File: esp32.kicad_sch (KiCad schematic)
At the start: 15 parts, among them J2 Conn_01x05_Pin, J3 PJ398SM-12, Q3 MMBT3904, Q4 MMBT3904, Y1 ECS-2520MV-xxx-xx

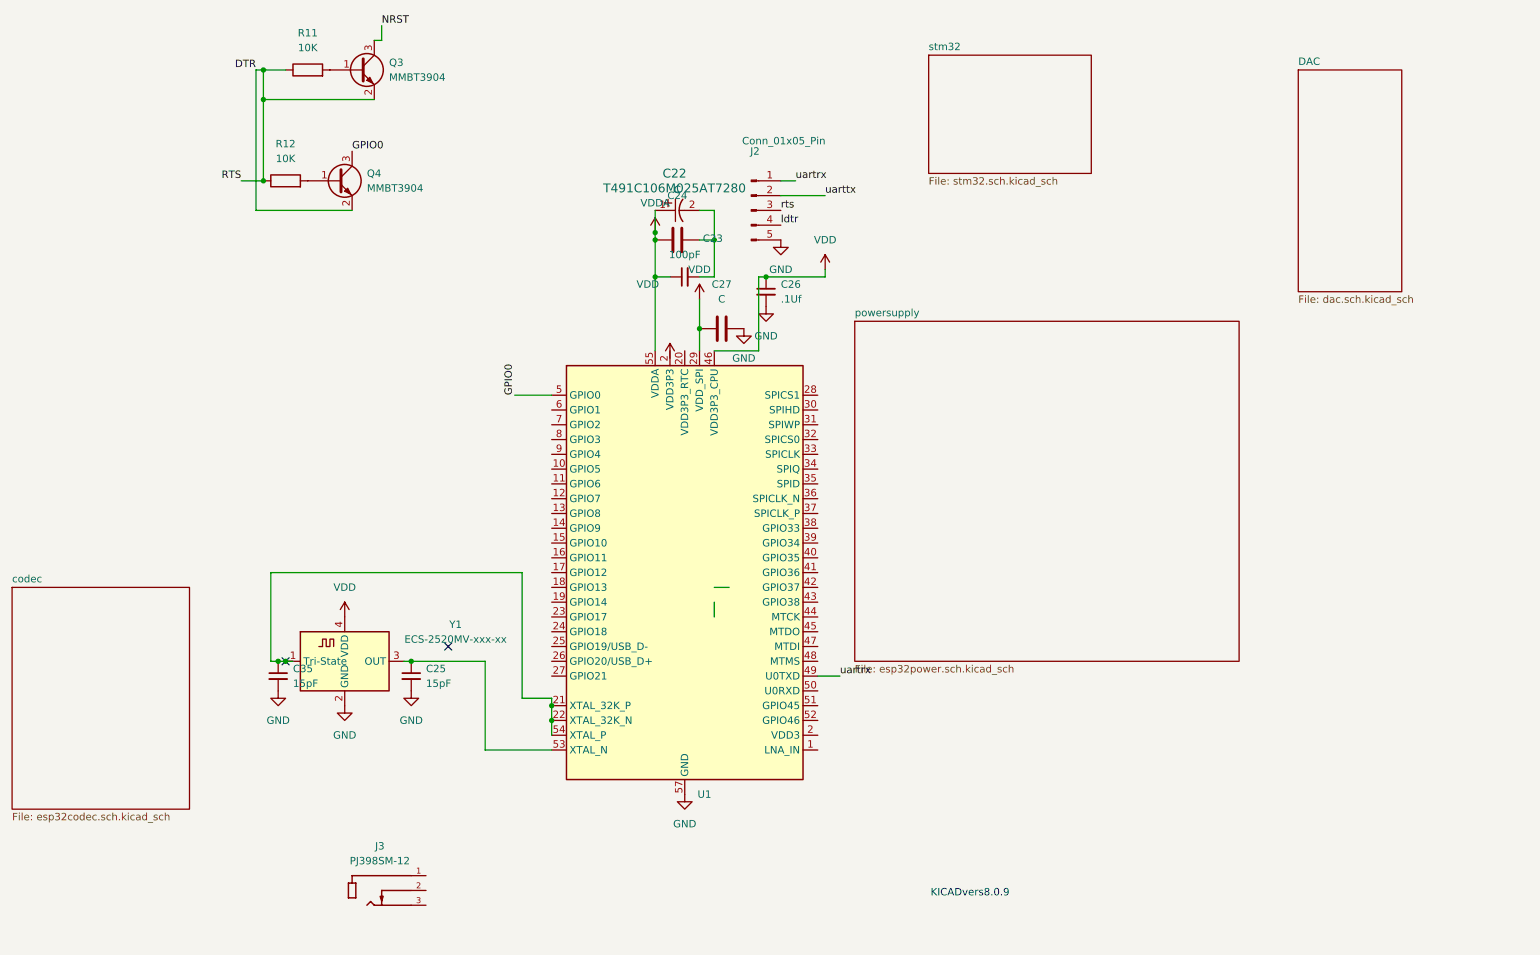
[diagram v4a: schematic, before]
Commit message: modelpathssdefuined
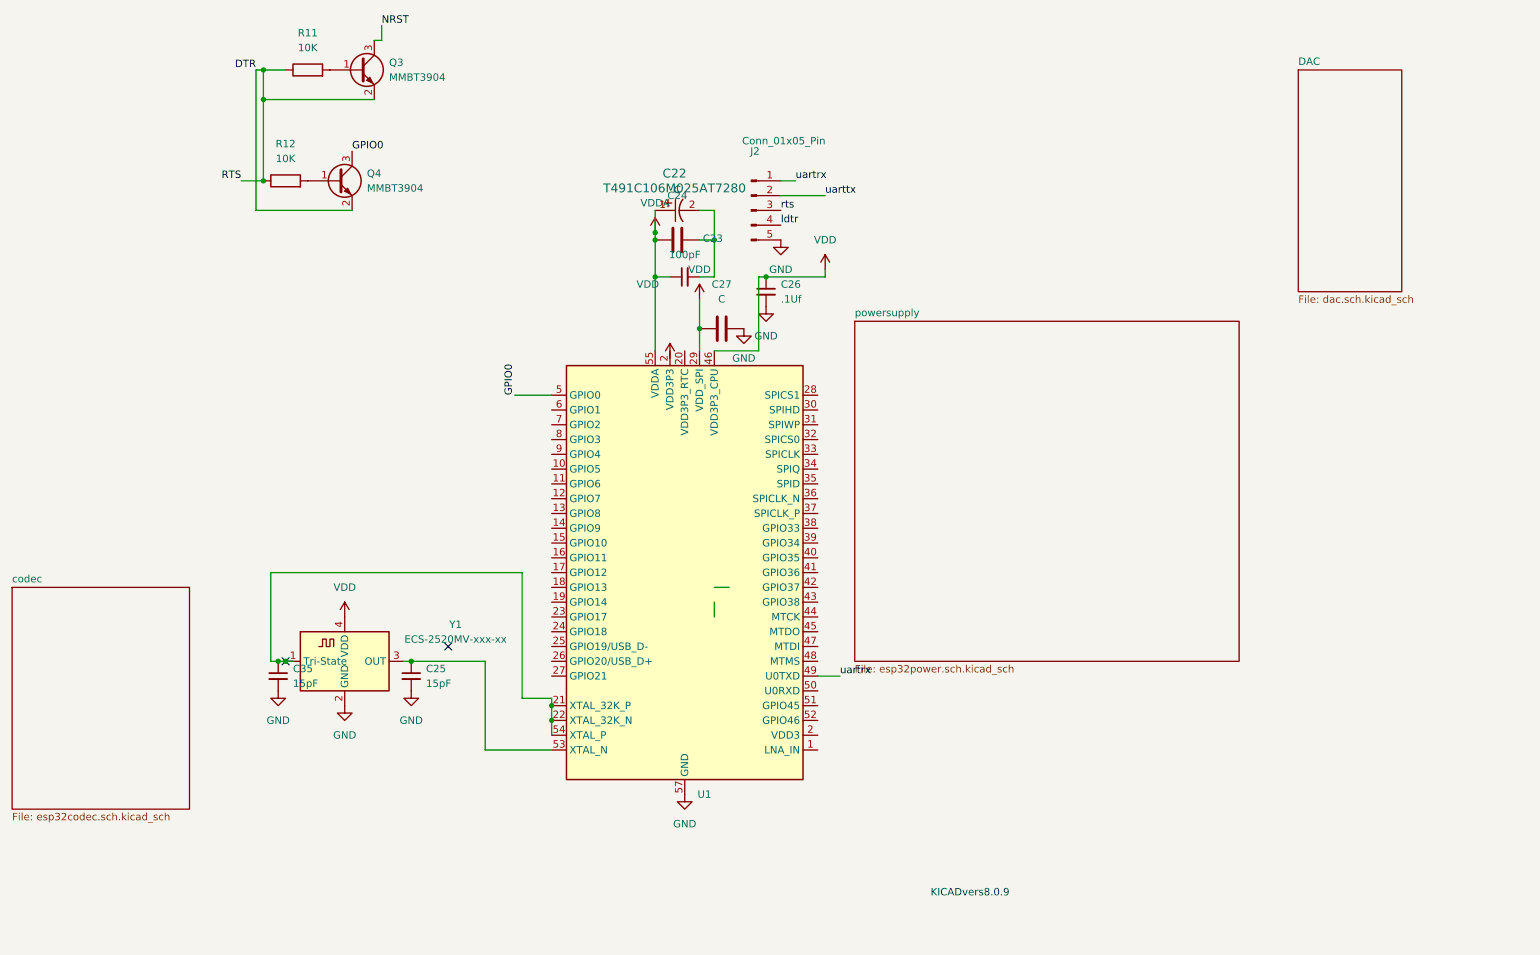
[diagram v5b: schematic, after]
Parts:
- removed J3: PJ398SM-12, customfootprints:THONK_PJ398SM-12, symbol esp32lib:PJ398SM-12
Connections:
- net at U1.2 (VDD3P3): now also U1.3 (VDD3P3)
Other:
- removed sheet stm32
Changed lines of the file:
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@@
-	)
-	(symbol
-		(lib_id "esp32lib:PJ398SM-12")
-		(at 86.36 168.91 0)
-		(unit 1)
-		(exclude_from_sim no)
-		(in_bom yes)
-		(on_board yes)
-		(dnp no)
-		(fields_autoplaced yes)
-		(property "Reference" "J3"
-			(at 86.0425 163.83 0)
-			(effects
-				(font
-					(size 1.27 1.27)
-				)
-			)
-		)
-		(property "Value" "PJ398SM-12"
-			(at 86.0425 166.37 0)
-			(effects
-				(font
-					(size 1.27 1.27)
-				)
-			)
-		)
-		(property "Footprint" "customfootprints:THONK_PJ398SM-12"
-			(at 86.36 168.91 0)
-			(effects
-				(font
-					(size 1.27 1.27)
-				)
-				(justify bottom)
-				(hide yes)
-			)
-		)
-		(property "Datasheet" ""
-			(at 86.36 168.91 0)
-			(effects
-				(font
-					(size 1.27 1.27)
-				)
-				(hide yes)
-			)
-		)
-		(property "Description" ""
-			(at 86.36 168.91 0)
-			(effects
-				(font
-					(size 1.27 1.27)
-				)
-				(hide yes)
-			)
-		)
-		(property "MF" "Thonk"
-			(at 86.36 168.91 0)
-			(effects
-				(font
-					(size 1.27 1.27)
-				)
-				(justify bottom)
-				(hide yes)
-			)
-		)
-		(property "MAXIMUM_PACKAGE_HEIGHT" "14.5 mm"
-			(at 86.36 168.91 0)
-			(effects
-				(font
-					(size 1.27 1.27)
-				)
-				(justify bottom)
-				(hide yes)
-			)
-		)
-		(property "Package" "Package"
-			(at 86.36 168.91 0)
-			(effects
-				(font
-					(size 1.27 1.27)
-				)
-				(justify bottom)
-				(hide yes)
-			)
-		)
-		(property "Price" "None"
-			(at 86.36 168.91 0)
-			(effects
-				(font
-					(size 1.27 1.27)
-				)
-				(justify bottom)
-				(hide yes)
-			)
-		)
-		(property "Check_prices" "https://www.snapeda.com/parts/PJ398SM-12/Thonk/view-part/?ref=eda"
-			(at 86.36 168.91 0)
-			(effects
-				(font
-					(size 1.27 1.27)
-				)
-				(justify bottom)
-				(hide yes)
-			)
-		)
-		(property "STANDARD" "Manufacturer Recommendations"
-			(at 86.36 168.91 0)
-			(effects
-				(font
-					(size 1.27 1.27)
-				)
-				(justify bottom)
-				(hide yes)
-			)
-		)
-		(property "PARTREV" "1"
-			(at 86.36 168.91 0)
-			(effects
-				(font
-					(size 1.27 1.27)
-				)
-				(justify bottom)
-				(hide yes)
-			)
-		)
-		(property "SnapEDA_Link" "https://www.snapeda.com/parts/PJ398SM-12/Thonk/view-part/?ref=snap"
-			(at 86.36 168.91 0)
-			(effects
-				(font
-					(size 1.27 1.27)
-				)
-				(justify bottom)
-				(hide yes)
-			)
-		)
-		(property "MP" "PJ398SM-12"
-			(at 86.36 168.91 0)
-			(effects
-				(font
-					(size 1.27 1.27)
-				)
-				(justify bottom)
-				(hide yes)
-			)
-		)
-		(property "Description_1" "\n                        \n                            3.5mm Switching Jack Socket\n                        \n"
-			(at 86.36 168.91 0)
-			(effects
-				(font
-					(size 1.27 1.27)
-				)
-				(justify bottom)
-				(hide yes)
-			)
-		)
-		(property "Availability" "Not in stock"
-			(at 86.36 168.91 0)
-			(effects
-				(font
-					(size 1.27 1.27)
-				)
-				(justify bottom)
-				(hide yes)
-			)
-		)
-		(property "MANUFACTURER" "Thonk"
-			(at 86.36 168.91 0)
-			(effects
-				(font
-					(size 1.27 1.27)
-				)
-				(justify bottom)
-				(hide yes)
-			)
-		)
-		(pin "3"
-		)
-		(pin "2"
-		)
-		(pin "1"
-		)
-		(instances
-			(project ""
-				(path "/c4754426-a41b-4341-9d09-2e389619f3d6"
-					(reference "J3")
-					(unit 1)
-				)
-			)
-		)
 	)
 	(symbol
@@
 				)
 			)
-		)
-	)
-	(sheet
-		(at 180.34 27.94)
-		(size 27.94 20.32)
-		(fields_autoplaced yes)
-		(stroke
-			(width 0.1524)
-			(type solid)
-		)
-		(fill
-			(color 0 0 0 0.0000)
-		)
-		(property "Sheetname" "stm32"
-			(at 180.34 27.2284 0)
-			(effects
-				(font
-					(size 1.27 1.27)
-				)
-				(justify left bottom)
-			)
-		)
-		(property "Sheetfile" "stm32.sch.kicad_sch"
-			(at 180.34 48.8446 0)
-			(effects
-				(font
-					(size 1.27 1.27)
-				)
-				(justify left top)
-			)
-		)
-		(instances
-			(project "esp32"
-				(path "/c4754426-a41b-4341-9d09-2e389619f3d6"
-					(page "6")
-				)
-			)

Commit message: improvedCVSumming buffers
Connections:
- net at U1.2 (VDD3P3): now also U1.3 (VDD3P3)
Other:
- added sheet ADCCVbuffer (CVBuffer.kicad_sch)
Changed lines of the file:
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@@
+	)
+	(sheet
+		(at 66.04 160.02)
+		(size 20.32 17.78)
+		(fields_autoplaced yes)
+		(stroke
+			(width 0.1524)
+			(type solid)
+		)
+		(fill
+			(color 0 0 0 0.0000)
+		)
+		(property "Sheetname" "ADCCVbuffer"
+			(at 66.04 159.3084 0)
+			(effects
+				(font
+					(size 1.27 1.27)
+				)
+				(justify left bottom)
+			)
+		)
+		(property "Sheetfile" "CVBuffer.kicad_sch"
+			(at 66.04 178.3846 0)
+			(effects
+				(font
+					(size 1.27 1.27)
+				)
+				(justify left top)
+			)
+		)
+		(instances
+			(project "esp32"
+				(path "/c4754426-a41b-4341-9d09-2e389619f3d6"
+					(page "10")
+				)
+			)
+		)
 	)
 	(sheet

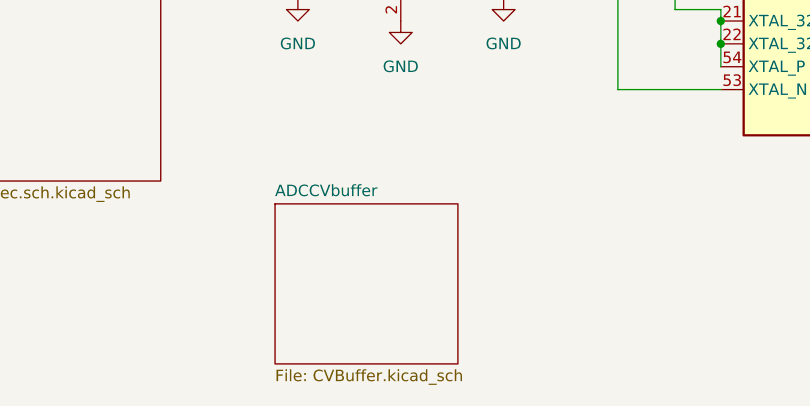
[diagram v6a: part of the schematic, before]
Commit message: added codec buffers
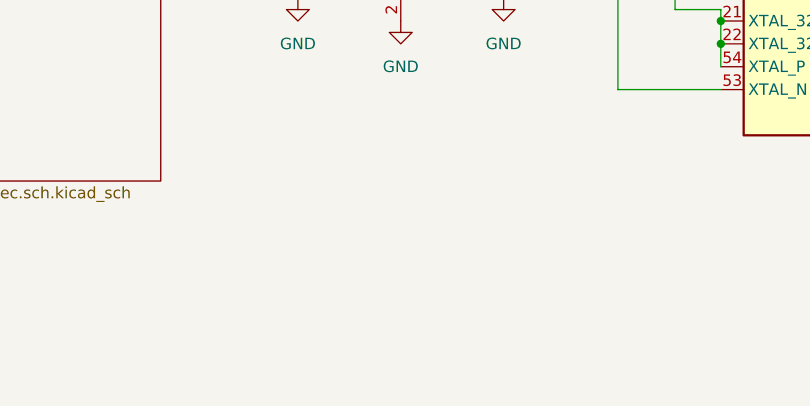
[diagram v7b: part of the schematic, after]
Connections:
- net at U1.2 (VDD3P3): now also U1.3 (VDD3P3)
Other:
- removed sheet ADCCVbuffer
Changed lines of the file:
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@@
-	)
-	(sheet
-		(at 66.04 160.02)
-		(size 20.32 17.78)
-		(fields_autoplaced yes)
-		(stroke
-			(width 0.1524)
-			(type solid)
-		)
-		(fill
-			(color 0 0 0 0.0000)
-		)
-		(property "Sheetname" "ADCCVbuffer"
-			(at 66.04 159.3084 0)
-			(effects
-				(font
-					(size 1.27 1.27)
-				)
-				(justify left bottom)
-			)
-		)
-		(property "Sheetfile" "CVBuffer.kicad_sch"
-			(at 66.04 178.3846 0)
-			(effects
-				(font
-					(size 1.27 1.27)
-				)
-				(justify left top)
-			)
-		)
-		(instances
-			(project "esp32"
-				(path "/c4754426-a41b-4341-9d09-2e389619f3d6"
-					(page "10")
-				)
-			)
-		)
 	)
 	(sheet

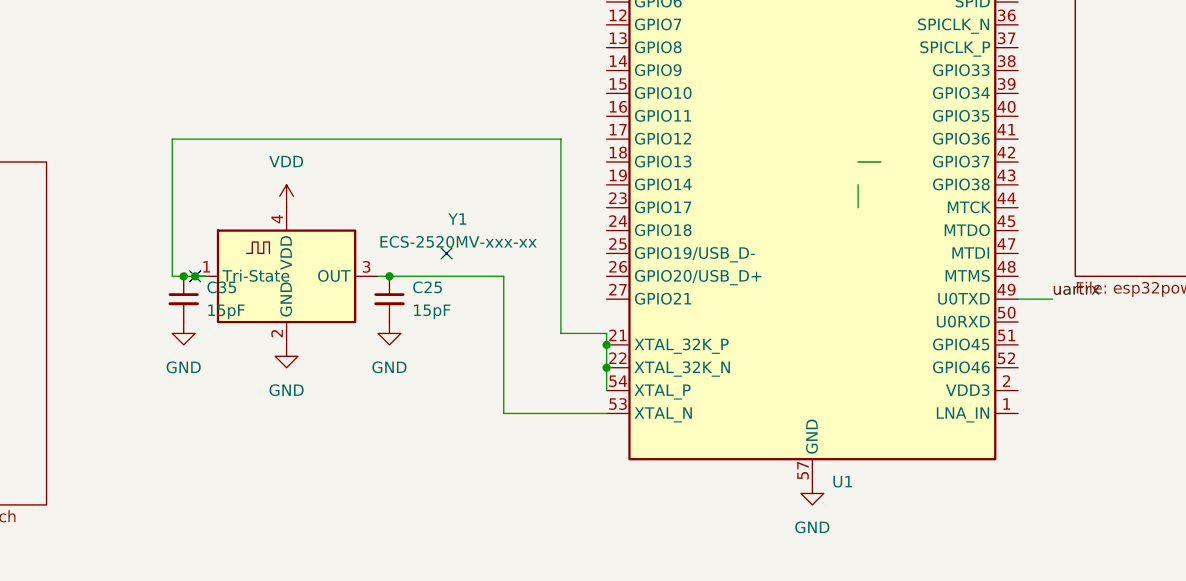
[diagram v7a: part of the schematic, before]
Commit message: added global library
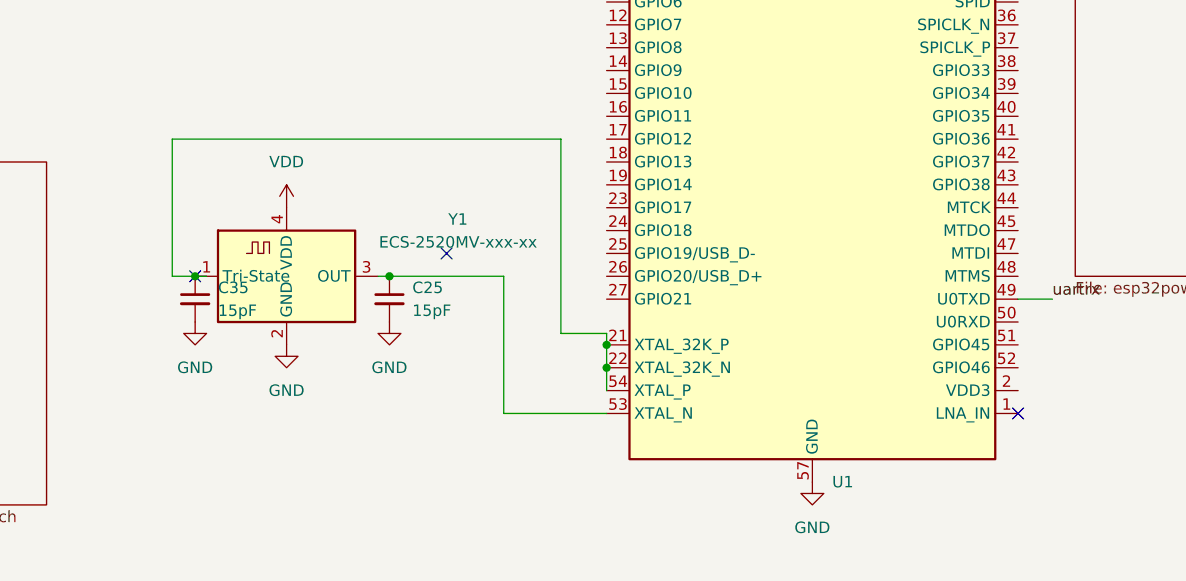
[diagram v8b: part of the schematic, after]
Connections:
- net at U1.2 (VDD3P3): now also U1.3 (VDD3P3)
- no-connect marks 2 -> 3
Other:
- moved on the sheet: C35
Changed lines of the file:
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@@
-	)
-	(junction
-		(at 68.58 132.08)
-		(diameter 0)
-		(color 0 0 0 0)
 	)
 	(junction
@@
 	)
 	(no_connect
+		(at 161.29 147.32)
+	)
+	(no_connect
 		(at 69.85 132.08)
 	)
@@
 	(wire
 		(pts
-			(xy 143.51 124.46) (xy 143.51 121.92)
-		)
-		(stroke
-			(width 0)
-			(type default)
-		)
-	)
-	(wire
-		(pts
 			(xy 133.35 59.69) (xy 133.35 66.04)
 		)
@@
 	(wire
 		(pts
-			(xy 146.05 119.38) (xy 143.51 119.38)
-		)
-		(stroke
-			(width 0)
-			(type default)
-		)
-	)
-	(wire
-		(pts
-			(xy 67.31 132.08) (xy 68.58 132.08)
+			(xy 67.31 132.08) (xy 69.85 132.08)
 		)
 		(stroke
@@
 		(pts
 			(xy 66.04 35.56) (xy 85.09 35.56)
-		)
-		(stroke
-			(width 0)
-			(type default)
-		)
-	)
-	(wire
-		(pts
-			(xy 68.58 132.08) (xy 69.85 132.08)
 		)
 		(stroke
@@
 	(symbol
 		(lib_id "Device:C_Small")
-		(at 68.58 134.62 0)
+		(at 69.85 134.62 0)
 		(unit 1)
 		(exclude_from_sim no)
@@
 		(fields_autoplaced yes)
 		(property "Reference" "C35"
-			(at 71.12 133.3562 0)
+			(at 72.39 133.3562 0)
 			(effects
 				(font
@@
 		)
 		(property "Value" "15pF"
-			(at 71.12 135.8962 0)
+			(at 72.39 135.8962 0)
 			(effects
 				(font
@@
 		)
 		(property "Footprint" "Capacitor_SMD:C_0201_0603Metric"
-			(at 68.58 134.62 0)
+			(at 69.85 134.62 0)
 			(effects
 				(font
@@
 		)
 		(property "Datasheet" "~"
-			(at 68.58 134.62 0)
+			(at 69.85 134.62 0)
 			(effects
 				(font
@@
 		)
 		(property "Description" "Unpolarized capacitor, small symbol"
-			(at 68.58 134.62 0)
+			(at 69.85 134.62 0)
 			(effects
 				(font
@@
 	(symbol
 		(lib_id "power:GND")
-		(at 68.58 137.16 0)
+		(at 69.85 137.16 0)
 		(unit 1)
 		(exclude_from_sim no)
@@
 		(fields_autoplaced yes)
 		(property "Reference" "#PWR76"
-			(at 68.58 143.51 0)
+			(at 69.85 143.51 0)
 			(effects
 				(font
@@
 		)
 		(property "Value" "GND"
-			(at 68.58 142.24 0)
+			(at 69.85 142.24 0)
 			(effects
 				(font
@@
 		)
 		(property "Footprint" ""
-			(at 68.58 137.16 0)
+			(at 69.85 137.16 0)
 			(effects
 				(font
@@
 		)
 		(property "Datasheet" ""
-			(at 68.58 137.16 0)
+			(at 69.85 137.16 0)
 			(effects
 				(font
@@
 		)
 		(property "Description" "Power symbol creates a global label with name \"GND\" , ground"
-			(at 68.58 137.16 0)
-			(effects
-				(font
+			(at 69.85 137.16 0)
+			(effects
+				(font
